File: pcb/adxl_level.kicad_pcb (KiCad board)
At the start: 2 copper layers, 111.8 x 96.5 mm, 14 parts, among them P1 CONN_01X06, U1 LM358N, U2 LM358N, U3 LM358N

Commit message: PCB designed
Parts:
- added U4: LM358N, Housings_DIP:DIP-8_W7.62mm, F.Cu at (133.3, 130.8)
- moved D2 160.0 mm to (146.1, 127.0)
- moved R7 150.1 mm to (135.9, 110.5)
- moved R6 141.5 mm to (130.8, 116.8), turned to 90 degrees
- moved R5 139.6 mm to (128.3, 76.2), turned to 0 degrees
- moved D1 132.6 mm to (161.3, 127.0), turned to 270 degrees
- moved U3 132.1 mm to (142.2, 102.9)
- moved U2 126.6 mm to (128.3, 85.1)
- moved R2 115.8 mm to (137.2, 118.1), turned to 0 degrees
- moved R4 113.2 mm to (156.2, 109.2), turned to 90 degrees
- moved R1 111.8 mm to (153.7, 124.5), turned to 270 degrees
- moved R3 110.0 mm to (146.1, 76.2), turned to 0 degrees
- moved U1 89.8 mm to (153.7, 92.7), turned to 180 degrees
- moved BT1 80.3 mm to (161.3, 108.0), turned to 90 degrees
- moved P1 62.0 mm to (166.4, 90.2), turned to 0 degrees
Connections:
- U2 pad 1: Net-(R1-Pad1) -> Net-(R5-Pad1)
- U2 pad 2: Net-(R1-Pad1) -> Net-(R3-Pad1)
- U2 pad 3: GND -> Net-(R1-Pad1)
- U2 pad 5: Net-(R1-Pad1) -> (no net)
- U2 pad 6: Net-(R3-Pad1) -> (no net)
- U2 pad 7: Net-(R5-Pad1) -> (no net)
- U3 pad 1: Net-(D1-Pad2) -> Net-(R1-Pad1)
- U3 pad 2: Net-(R6-Pad1) -> Net-(R1-Pad1)
- U3 pad 3: Net-(R1-Pad1) -> GND
- U3 pad 5: Net-(R5-Pad1) -> (no net)
- U3 pad 6: Net-(R7-Pad1) -> (no net)
- U3 pad 7: Net-(D2-Pad2) -> (no net)
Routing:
- net +9V: track 0.00 -> 113.2 mm
- net Net-(R1-Pad1): track 0.00 -> 76.9 mm
- net Net-(R5-Pad1): track 0.00 -> 54.6 mm
- net GND: track 0.00 -> 45.5 mm, vias 0 -> 4
- net /Yout: track 0.00 -> 36.9 mm
- net Net-(R3-Pad2): track 0.00 -> 31.9 mm
- net Net-(D1-Pad2): track 0.00 -> 30.3 mm
- net Net-(R3-Pad1): track 0.00 -> 24.0 mm
- net Net-(R7-Pad1): track 0.00 -> 22.4 mm
- net Net-(D2-Pad2): track 0.00 -> 20.8 mm
- net Net-(R4-Pad2): track 0.00 -> 16.4 mm
- net /Xout: track 0.00 -> 13.8 mm
- net Net-(R6-Pad1): track 0.00 -> 12.5 mm
- added copper zone on F.Cu, net GND
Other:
- board size 111.8 x 96.5 mm -> 101.6 x 76.2 mm

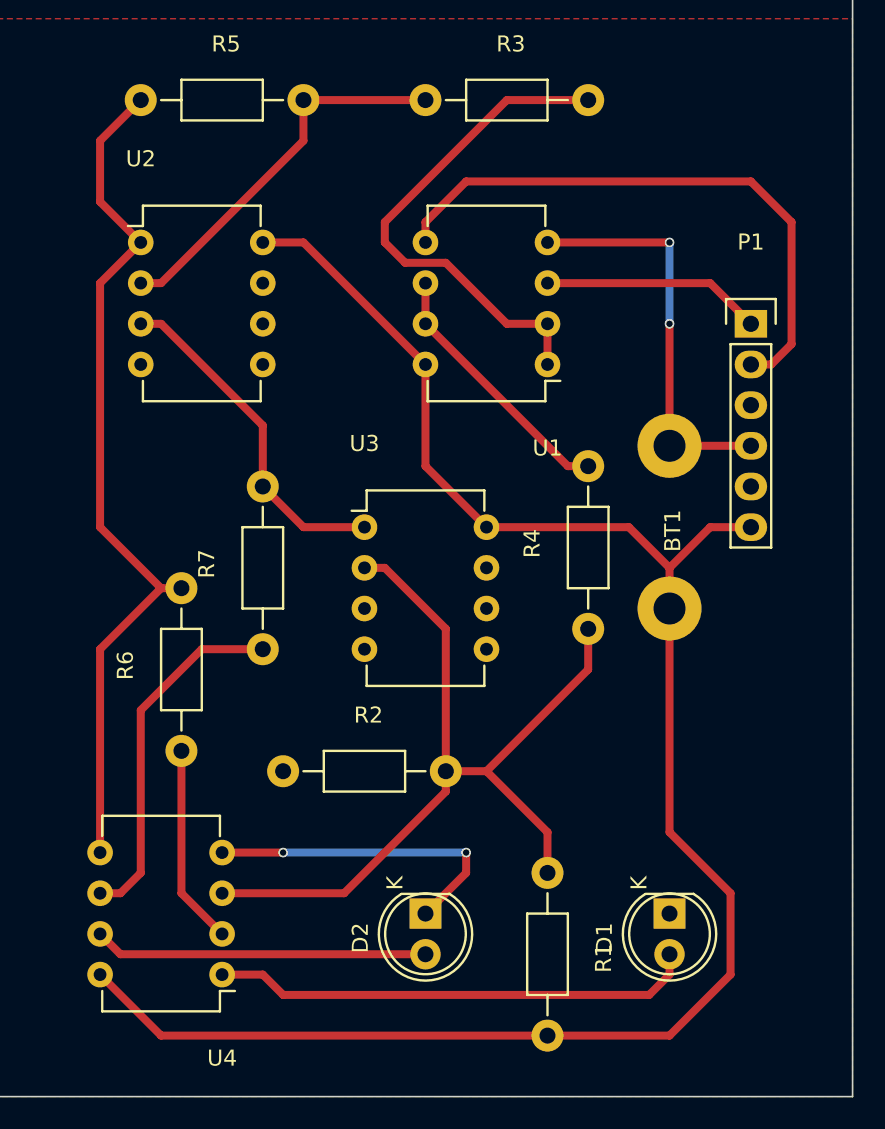
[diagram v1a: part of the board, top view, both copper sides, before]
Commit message: Fixed too narrow connections
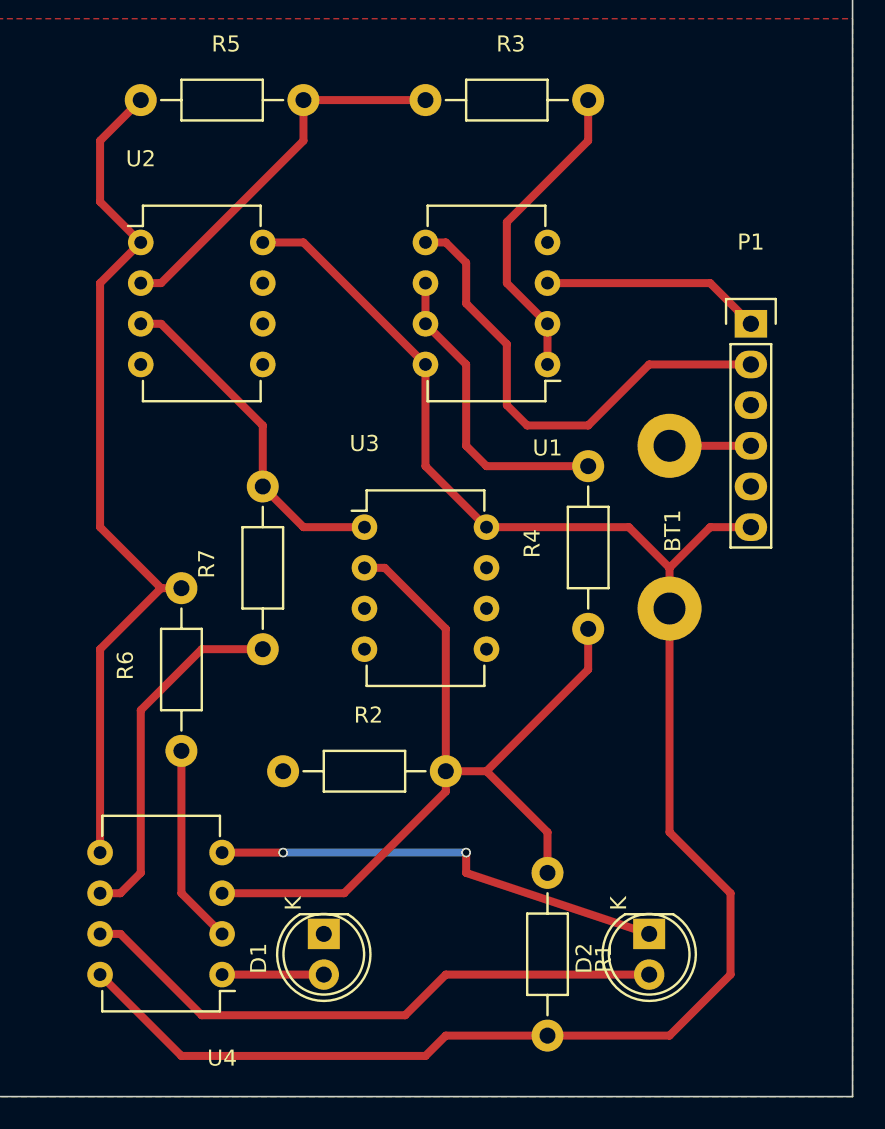
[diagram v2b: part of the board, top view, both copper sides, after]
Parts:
- moved D1 21.6 mm to (139.7, 128.3)
- moved D2 14.0 mm to (160.0, 128.3)
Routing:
- net Net-(D1-Pad2): track 30.3 -> 6.35 mm
- net Net-(D2-Pad2): track 20.8 -> 37.4 mm
- net Net-(R3-Pad2): track 31.9 -> 19.7 mm
- net GND: track 45.5 -> 33.6 mm, vias 4 -> 2
- net /Yout: track 36.9 -> 30.4 mm
- net Net-(R4-Pad2): track 16.4 -> 19.4 mm
- net +9V: track 113.2 -> 114.2 mm

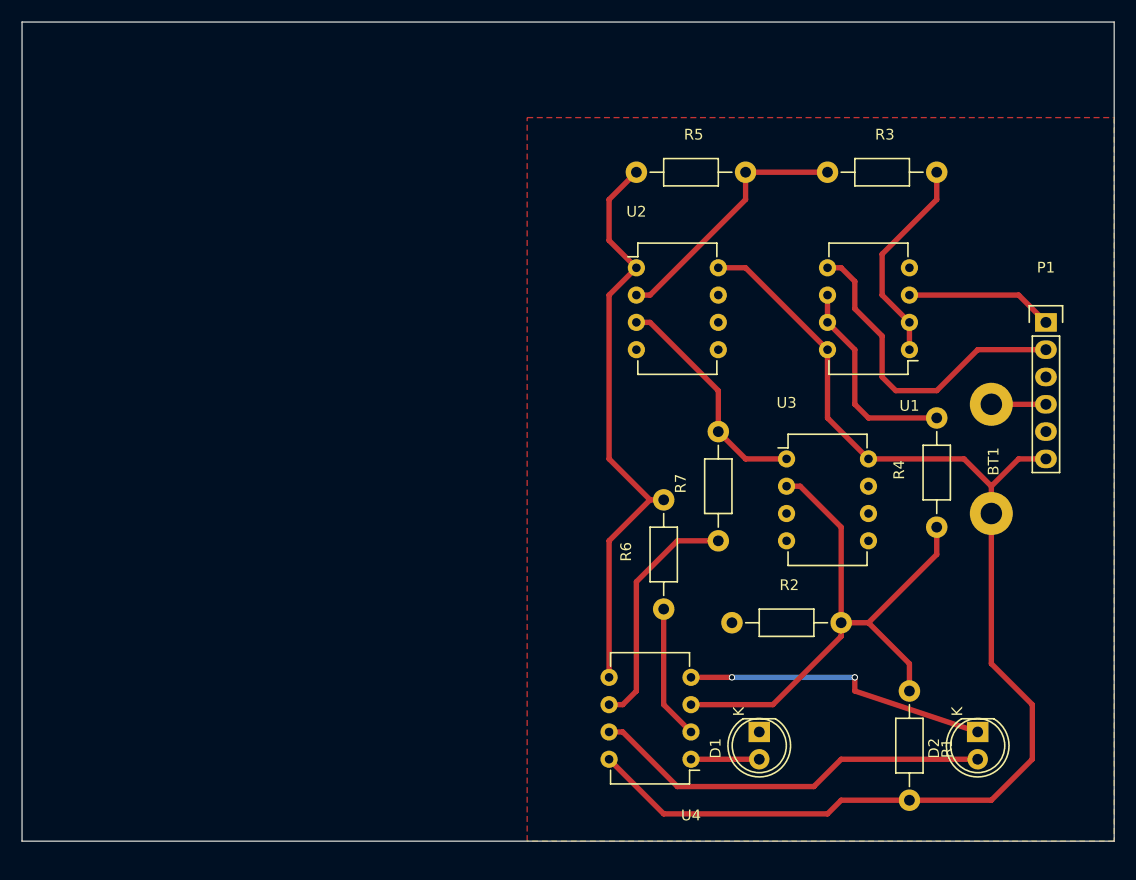
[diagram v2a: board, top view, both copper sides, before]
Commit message: Optimize connection and traces
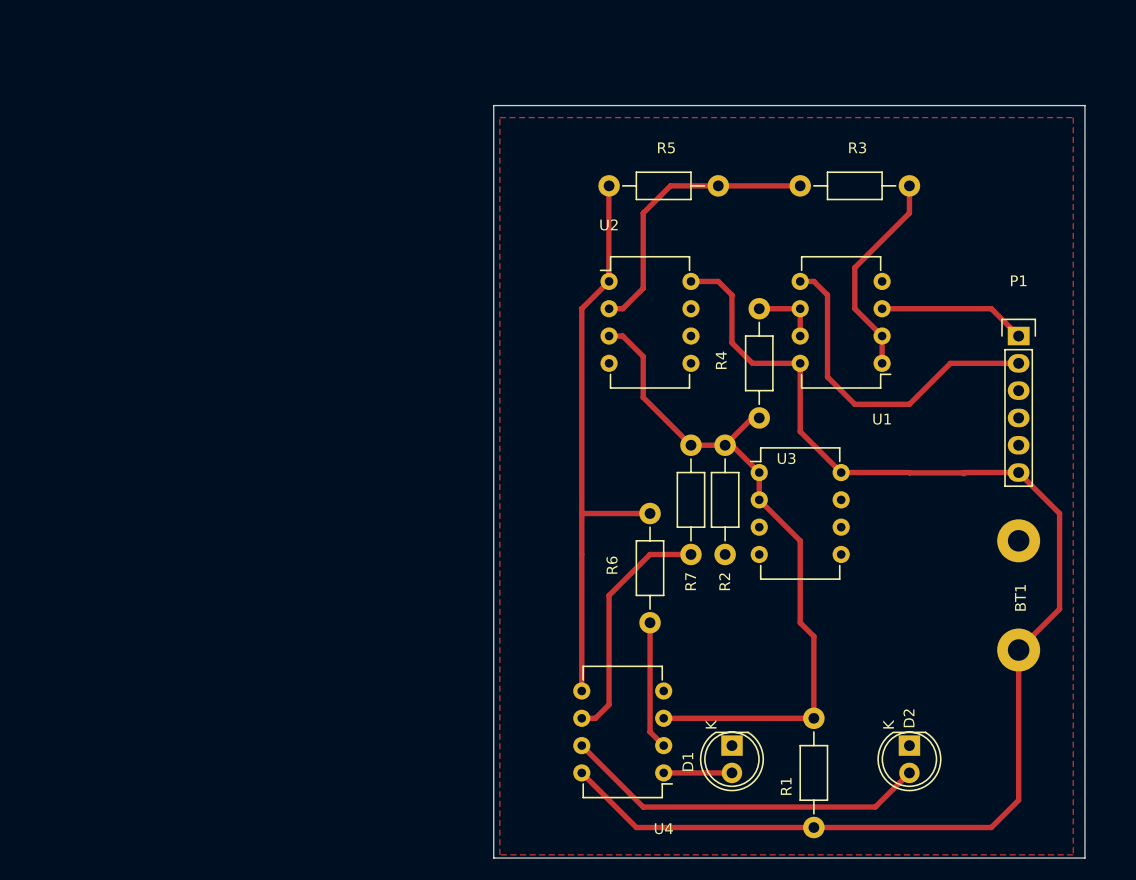
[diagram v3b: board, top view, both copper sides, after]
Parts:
- moved R4 19.4 mm to (139.7, 99.1)
- moved BT1 13.0 mm to (163.8, 120.7)
- moved R1 9.25 mm to (144.8, 127.0)
- moved D2 6.48 mm to (153.7, 129.5)
- moved R2 6.38 mm to (136.5, 111.8), turned to 90 degrees
- moved R3 2.84 mm to (143.5, 77.5)
- moved U3 2.84 mm to (139.7, 104.1)
- moved R5 2.84 mm to (125.7, 77.5)
- moved U2 2.84 mm to (125.7, 86.4)
- moved R7 2.84 mm to (133.3, 111.8)
- moved U1 2.84 mm to (151.1, 94.0)
- moved U4 2.84 mm to (130.8, 132.1)
- moved P1 2.84 mm to (163.8, 91.4)
- moved D1 2.84 mm to (137.2, 129.5)
- moved R6 1.80 mm to (129.5, 118.1)
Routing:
- net GND: track 33.6 -> 0.00 mm, vias 2 -> 0
- net Net-(R4-Pad2): track 19.4 -> 6.35 mm
- net Net-(R1-Pad1): track 76.9 -> 64.6 mm
- net +9V: track 114.2 -> 121.8 mm
- net Net-(D2-Pad2): track 37.4 -> 34.2 mm
- net Net-(R3-Pad1): track 24.0 -> 26.6 mm
- net /Yout: track 30.4 -> 31.1 mm
- net Net-(R6-Pad1): track 12.5 -> 12.0 mm
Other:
- board size 101.6 x 76.2 mm -> 55 x 70 mm
